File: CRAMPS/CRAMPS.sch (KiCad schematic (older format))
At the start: 11 parts, among them M101 LOGO_OSHW, M102 PCB_GREEN_RMC, P102 RESET, P103 SERIAL0, P104 POWER, Q101 2N7002, SW101 RESET, SW102 POWER, U4 BEAGLEBONEBLACK

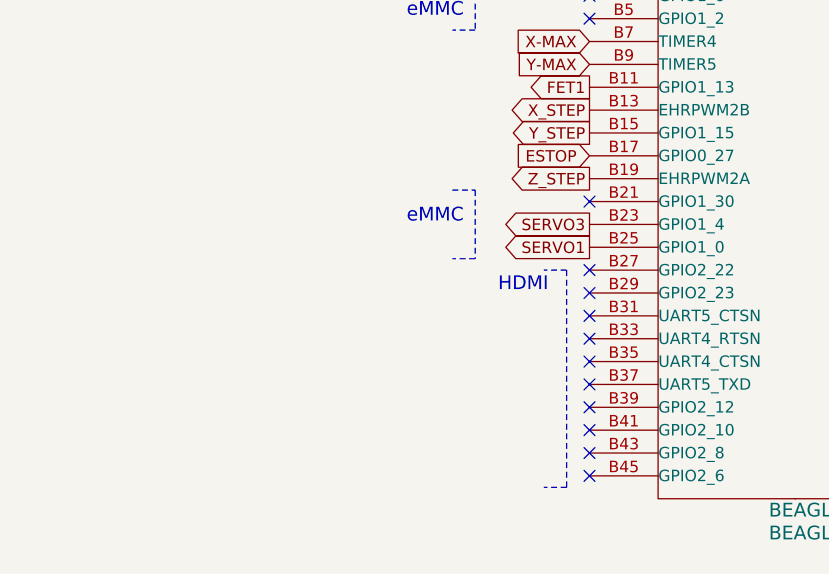
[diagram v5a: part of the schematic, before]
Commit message: Initial BOM files for PCB version 1.0 Added README and ToDo text files
Signed-off-by: Charles Steinkuehler <charles@steinkuehler.net>
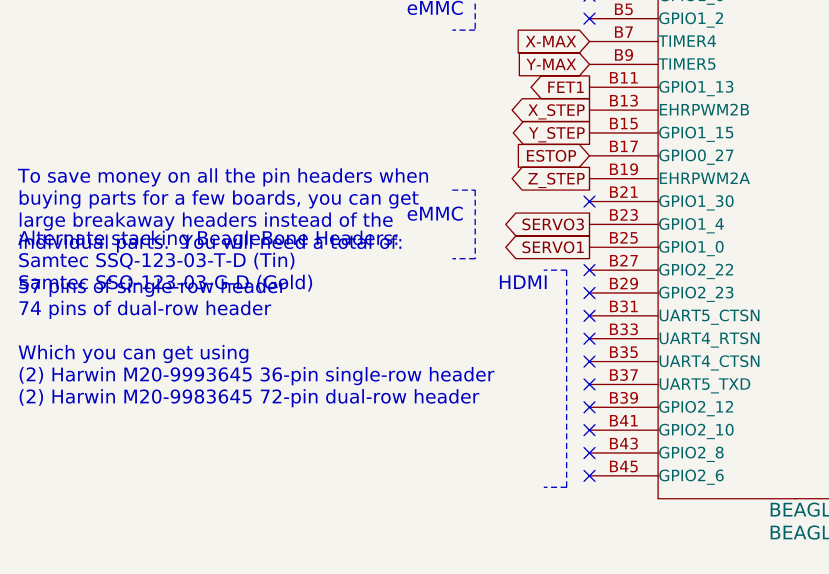
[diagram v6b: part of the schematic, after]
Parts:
- D101: Mfg (none) -> Osram; PartNo (none) -> LG R971-KN-1
- P102, P104: Mfg (none) -> Harwin; PartNo (none) -> M20-9990245
- P103: Mfg (none) -> Harwin; PartNo (none) -> M20-7820646
- Q101: Mfg (none) -> Diodes Inc.; PartNo (none) -> 2N7002K-7
- R101: Mfg (none) -> KOA; PartNo (none) -> RK73H2ATTDD3300F
- SW101, SW102: Mfg (none) -> TE; PartNo (none) -> FSM2JH
- U4: Mfg (none) -> Major League; Note (none) -> 2x required!; PartNo (none) -> SSHQ-123-D-08-GT-LF
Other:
- note added: "Alternate stacking BeagleBone Headers:\nSamtec SSQ-123-03-T-D (Tin)\nSamtec SSQ-123-03-G-D (Gold)\n"
- note added: "To save money on all the pin headers when\nbuying parts for a few boards, you can get\nlarge breakaway headers instead of the\nindividual parts. You will need a total of:\n\n57 pins of single-row header\n74 pins of dual-row header\n\nWhich you can get using\n(2) Harwin M20-9993645 36-pin single-row header\n(2) Harwin M20-9983645 72-pin dual-row header\n"
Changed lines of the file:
@@
 Sheet 1 10
 Title "CRAMPS (Cape-RAMPS for BeagleBone)"
-Date "9 feb 2014"
+Date "11 feb 2014"
 Rev "v1.0"
 Comp ""
@@
 F 2 "" H 10000 5000 60  0001 C CNN
 F 3 "" H 10000 5000 60  0001 C CNN
+F 4 "TE" H 6250 6550 60  0001 C CNN "Mfg"
+F 5 "FSM2JH" H 6250 6550 60  0001 C CNN "PartNo"
 	1    10000 5000
 	0    1    1    0
@@
 F 2 "" H 7900 5000 60  0001 C CNN
 F 3 "" H 7900 5000 60  0001 C CNN
+F 4 "Osram" H 6250 6550 60  0001 C CNN "Mfg"
+F 5 "LG R971-KN-1" H 6250 6550 60  0001 C CNN "PartNo"
 	1    7900 5000
 	0    1    1    0
@@
 F 2 "" H 7900 4450 60  0001 C CNN
 F 3 "" H 7900 4450 60  0001 C CNN
+F 4 "KOA" H 6250 6550 60  0001 C CNN "Mfg"
+F 5 "RK73H2ATTDD3300F" H 6250 6550 60  0001 C CNN "PartNo"
 	1    7900 4450
 	1    0    0    -1
@@
 F 2 "" H 10750 5000 60  0000 C CNN
 F 3 "" H 10750 5000 60  0000 C CNN
+F 4 "Harwin" H 6250 6550 60  0001 C CNN "Mfg"
+F 5 "M20-9990245" H 6250 6550 60  0001 C CNN "PartNo"
 	1    10750 5000
 	1    0    0    -1
@@
 F 2 "~" H 7800 5600 60  0000 C CNN
 F 3 "~" H 7800 5600 60  0000 C CNN
+F 4 "Diodes Inc." H 6250 6550 60  0001 C CNN "Mfg"
+F 5 "2N7002K-7" H 6250 6550 60  0001 C CNN "PartNo"
 	1    7800 5600
 	1    0    0    -1
@@
 F 2 "~" H 3450 600 60  0000 C CNN
 F 3 "~" H 3450 600 60  0000 C CNN
+F 4 "Major League" H 3650 5050 60  0001 C CNN "Mfg"
+F 5 "SSHQ-123-D-08-GT-LF" H 3650 5050 60  0001 C CNN "PartNo"
+F 6 "2x required!" H 3650 5050 60  0001 C CNN "Note"
 	1    3650 1850
 	1    0    0    -1
@@
 F 2 "~" H 4150 600 60  0000 C CNN
 F 3 "~" H 4150 600 60  0000 C CNN
+F 4 "Major League" H 3650 5050 60  0001 C CNN "Mfg"
+F 5 "SSHQ-123-D-08-GT-LF" H 3650 5050 60  0001 C CNN "PartNo"
+F 6 "2x required!" H 3650 5050 60  0001 C CNN "Note"
 	2    4350 1850
 	-1   0    0    -1
@@
 F 2 "~" H 3450 3800 60  0000 C CNN
 F 3 "~" H 3450 3800 60  0000 C CNN
+F 4 "Major League" H 3650 5050 60  0001 C CNN "Mfg"
+F 5 "SSHQ-123-D-08-GT-LF" H 3650 5050 60  0001 C CNN "PartNo"
+F 6 "2x required!" H 3650 5050 60  0001 C CNN "Note"
 	3    3650 5050
 	1    0    0    -1
@@
 F 2 "~" H 4150 3800 60  0000 C CNN
 F 3 "~" H 4150 3800 60  0000 C CNN
+F 4 "Major League" H 3650 5050 60  0001 C CNN "Mfg"
+F 5 "SSHQ-123-D-08-GT-LF" H 3650 5050 60  0001 C CNN "PartNo"
+F 6 "2x required!" H 3650 5050 60  0001 C CNN "Note"
 	4    4350 5050
 	-1   0    0    -1
@@
 F 2 "" H 2050 6950 60  0001 C CNN
 F 3 "" H 2050 6950 60  0001 C CNN
+F 4 "Harwin" H 6250 6550 60  0001 C CNN "Mfg"
+F 5 "M20-7820646" H 6250 6550 60  0001 C CNN "PartNo"
 	1    2050 6950
 	1    0    0    -1
@@
 F 2 "" H 10000 3700 60  0001 C CNN
 F 3 "" H 10000 3700 60  0001 C CNN
+F 4 "TE" H 6250 6550 60  0001 C CNN "Mfg"
+F 5 "FSM2JH" H 6250 6550 60  0001 C CNN "PartNo"
 	1    10000 3700
 	0    1    1    0
@@
 F 2 "" H 10750 3700 60  0000 C CNN
 F 3 "" H 10750 3700 60  0000 C CNN
+F 4 "Harwin" H 6250 6550 60  0001 C CNN "Mfg"
+F 5 "M20-9990245" H 6250 6550 60  0001 C CNN "PartNo"
 	1    10750 3700
 	1    0    0    -1
@@
 NoConn ~ 3100 3000
 NoConn ~ 4900 1700
+Text Notes 600  2200 0    60   ~ 0
+Alternate stacking BeagleBone Headers:\nSamtec SSQ-123-03-T-D (Tin)\nSamtec SSQ-123-03-G-D (Gold)\n
+Text Notes 600  2700 0    60   ~ 0
+To save money on all the pin headers when\nbuying parts for a few boards, you can get\nlarge breakaway headers instead of the\nindividual parts.  You will need a total of:\n\n57 pins of single-row header\n74 pins of dual-row header\n\nWhich you can get using\n(2) Harwin M20-9993645 36-pin single-row header\n(2) Harwin M20-9983645 72-pin dual-row header\n
 $EndSCHEMATC

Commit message: BOM Updates Fixed incorrect Molex part number Added Stackpole resistor part numbers Switched to value-sorted BOM export from KiCAD Modified some attribute fields to get same-value parts to list on a single BOM line
Signed-off-by: Charles Steinkuehler <charles@steinkuehler.net>
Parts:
- R101: AltMfg (none) -> KOA; AltPartNo (none) -> RK73H2ATTDD3300F; Mfg KOA -> Stackpole; PartNo RK73H2ATTDD3300F -> RMCF0805FT330R
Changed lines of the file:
@@
 Sheet 1 10
 Title "CRAMPS (Cape-RAMPS for BeagleBone)"
-Date "11 feb 2014"
+Date "15 feb 2014"
 Rev "v1.0"
 Comp ""
@@
 F 2 "OSHW_logo_2" H 6000 7250 60  0000 C CNN
 F 3 "" H 6100 7200 60  0001 C CNN
-	1    6100 7200
-	1    0    0    -1
+    1    6100 7200
+    1    0    0    -1
 $EndComp
 Text GLabel 4900 5900 2    50   Input ~ 0
@@
 F 2 "" H 10000 5500 60  0001 C CNN
 F 3 "" H 10000 5500 60  0001 C CNN
-	1    10000 5500
-	1    0    0    -1
+    1    10000 5500
+    1    0    0    -1
 $EndComp
 $Comp
@@
 F 4 "TE" H 6250 6550 60  0001 C CNN "Mfg"
 F 5 "FSM2JH" H 6250 6550 60  0001 C CNN "PartNo"
-	1    10000 5000
-	0    1    1    0
+    1    10000 5000
+    0    1    1    0
 $EndComp
 $Comp
@@
 F 2 "" H 7900 6000 60  0001 C CNN
 F 3 "" H 7900 6000 60  0001 C CNN
-	1    7900 6000
-	1    0    0    -1
+    1    7900 6000
+    1    0    0    -1
 $EndComp
 $Comp
@@
 F 4 "Osram" H 6250 6550 60  0001 C CNN "Mfg"
 F 5 "LG R971-KN-1" H 6250 6550 60  0001 C CNN "PartNo"
-	1    7900 5000
-	0    1    1    0
+    1    7900 5000
+    0    1    1    0
 $EndComp
 $Comp
@@
 F 2 "" H 7900 4450 60  0001 C CNN
 F 3 "" H 7900 4450 60  0001 C CNN
-F 4 "KOA" H 6250 6550 60  0001 C CNN "Mfg"
-F 5 "RK73H2ATTDD3300F" H 6250 6550 60  0001 C CNN "PartNo"
-	1    7900 4450
-	1    0    0    -1
+F 4 "Stackpole" H 6250 6550 60  0001 C CNN "Mfg"
+F 5 "RMCF0805FT330R" H 6250 6550 60  0001 C CNN "PartNo"
+F 6 "KOA" H 6250 6550 60  0001 C CNN "AltMfg"
+F 7 "RK73H2ATTDD3300F" H 6250 6550 60  0001 C CNN "AltPartNo"
+    1    7900 4450
+    1    0    0    -1
 $EndComp
 $Comp
@@
 F 2 "" H 5200 7200 60  0000 C CNN
 F 3 "" H 5200 7200 60  0000 C CNN
-	1    5200 7200
-	1    0    0    -1
+    1    5200 7200
+    1    0    0    -1
 $EndComp
 Text GLabel 4900 5300 2    50   Output ~ 0
@@
 F 4 "Harwin" H 6250 6550 60  0001 C CNN "Mfg"
 F 5 "M20-9990245" H 6250 6550 60  0001 C CNN "PartNo"
-	1    10750 5000
-	1    0    0    -1
+    1    10750 5000
+    1    0    0    -1
 $EndComp
 $Sheet
@@
 F 2 "" H 7900 4100 60  0000 C CNN
 F 3 "" H 7900 4100 60  0000 C CNN
-	1    7900 4100
-	1    0    0    -1
+    1    7900 4100
+    1    0    0    -1
 $EndComp
 $Comp
@@
 F 4 "Diodes Inc." H 6250 6550 60  0001 C CNN "Mfg"
 F 5 "2N7002K-7" H 6250 6550 60  0001 C CNN "PartNo"
-	1    7800 5600
-	1    0    0    -1
+    1    7800 5600
+    1    0    0    -1
 $EndComp
 Text Notes 5050 2200 0    60   ~ 0
@@
 F 5 "SSHQ-123-D-08-GT-LF" H 3650 5050 60  0001 C CNN "PartNo"
 F 6 "2x required!" H 3650 5050 60  0001 C CNN "Note"
-	1    3650 1850
-	1    0    0    -1
+    1    3650 1850
+    1    0    0    -1
 $EndComp
 $Comp
@@
 F 5 "SSHQ-123-D-08-GT-LF" H 3650 5050 60  0001 C CNN "PartNo"
 F 6 "2x required!" H 3650 5050 60  0001 C CNN "Note"
-	2    4350 1850
-	-1   0    0    -1
+    2    4350 1850
+    -1   0    0    -1
 $EndComp
 $Comp
@@
 F 5 "SSHQ-123-D-08-GT-LF" H 3650 5050 60  0001 C CNN "PartNo"
 F 6 "2x required!" H 3650 5050 60  0001 C CNN "Note"
-	3    3650 5050
-	1    0    0    -1
+    3    3650 5050
+    1    0    0    -1
 $EndComp
 $Comp
@@
 F 5 "SSHQ-123-D-08-GT-LF" H 3650 5050 60  0001 C CNN "PartNo"
 F 6 "2x required!" H 3650 5050 60  0001 C CNN "Note"
-	4    4350 5050
-	-1   0    0    -1
+    4    4350 5050
+    -1   0    0    -1
 $EndComp
 Text GLabel 3100 5100 0    50   Output ~ 0
@@
 F 4 "Harwin" H 6250 6550 60  0001 C CNN "Mfg"
 F 5 "M20-7820646" H 6250 6550 60  0001 C CNN "PartNo"
-	1    2050 6950
-	1    0    0    -1
+    1    2050 6950
+    1    0    0    -1
 $EndComp
 $Comp
@@
 F 2 "" H 1600 7300 60  0001 C CNN
 F 3 "" H 1600 7300 60  0001 C CNN
-	1    1600 7300
-	1    0    0    -1
-$EndComp
-Wire Wire Line
-	10000 5300 10000 5500
-Wire Wire Line
-	7900 5800 7900 6000
-Wire Wire Line
-	7900 4800 7900 4700
-Wire Wire Line
-	9800 4600 10400 4600
-Wire Wire Line
-	10000 4600 10000 4700
-Wire Notes Line
-	6500 650  6500 7600
-Wire Wire Line
-	10400 4600 10400 4900
+    1    1600 7300
+    1    0    0    -1
+$EndComp
+Wire Wire Line
+    10000 5300 10000 5500
+Wire Wire Line
+    7900 5800 7900 6000
+Wire Wire Line
+    7900 4800 7900 4700
+Wire Wire Line
+    9800 4600 10400 4600
+Wire Wire Line
+    10000 4600 10000 4700
+Wire Notes Line
+    6500 650  6500 7600
+Wire Wire Line
+    10400 4600 10400 4900
 Connection ~ 10000 4600
 Wire Wire Line
-	10400 5100 10400 5400
-Wire Wire Line
-	10400 5400 10000 5400
+    10400 5100 10400 5400
+Wire Wire Line
+    10400 5400 10000 5400
 Connection ~ 10000 5400
 Wire Wire Line
-	7900 4100 7900 4200
-Wire Wire Line
-	7900 5400 7900 5200
-Wire Notes Line
-	5500 850  5400 850
-Wire Notes Line
-	5400 850  5400 1050
-Wire Notes Line
-	5400 1050 5500 1050
-Wire Notes Line
-	2500 850  2600 850
-Wire Notes Line
-	2600 850  2600 1050
-Wire Notes Line
-	2600 1050 2500 1050
-Wire Notes Line
-	5500 1650 5400 1650
-Wire Notes Line
-	5400 1650 5400 1950
-Wire Notes Line
-	5400 1950 5500 1950
-Wire Notes Line
-	2500 1750 2600 1750
-Wire Notes Line
-	3000 2100 3000 3050
-Wire Notes Line
-	5000 3050 5100 3050
-Wire Notes Line
-	3000 3050 2900 3050
-Wire Notes Line
-	3000 2100 2900 2100
-Wire Notes Line
-	5000 2100 5000 3050
-Wire Notes Line
-	5000 2100 5100 2100
-Wire Wire Line
-	1700 6700 1600 6700
-Wire Wire Line
-	1600 6700 1600 7300
-Wire Wire Line
-	1500 7000 1700 7000
-Wire Wire Line
-	1700 7100 1500 7100
+    7900 4100 7900 4200
+Wire Wire Line
+    7900 5400 7900 5200
+Wire Notes Line
+    5500 850  5400 850
+Wire Notes Line
+    5400 850  5400 1050
+Wire Notes Line
+    5400 1050 5500 1050
+Wire Notes Line
+    2500 850  2600 850
+Wire Notes Line
+    2600 850  2600 1050
+Wire Notes Line
+    2600 1050 2500 1050
+Wire Notes Line
+    5500 1650 5400 1650
+Wire Notes Line
+    5400 1650 5400 1950
+Wire Notes Line
+    5400 1950 5500 1950
+Wire Notes Line
+    2500 1750 2600 1750
+Wire Notes Line
+    3000 2100 3000 3050
+Wire Notes Line
+    5000 3050 5100 3050
+Wire Notes Line
+    3000 3050 2900 3050
+Wire Notes Line
+    3000 2100 2900 2100
+Wire Notes Line
+    5000 2100 5000 3050
+Wire Notes Line
+    5000 2100 5100 2100
+Wire Wire Line
+    1700 6700 1600 6700
+Wire Wire Line
+    1600 6700 1600 7300
+Wire Wire Line
+    1500 7000 1700 7000
+Wire Wire Line
+    1700 7100 1500 7100
 Text GLabel 4900 4300 2    50   UnSpc ~ 0
 SYS_5V
@@
 F 2 "" H 10000 4200 60  0001 C CNN
 F 3 "" H 10000 4200 60  0001 C CNN
-	1    10000 4200
-	1    0    0    -1
+    1    10000 4200
+    1    0    0    -1
 $EndComp
 $Comp
@@
 F 4 "TE" H 6250 6550 60  0001 C CNN "Mfg"
 F 5 "FSM2JH" H 6250 6550 60  0001 C CNN "PartNo"
-	1    10000 3700
-	0    1    1    0
+    1    10000 3700
+    0    1    1    0
 $EndComp
 $Comp
@@
 F 4 "Harwin" H 6250 6550 60  0001 C CNN "Mfg"
 F 5 "M20-9990245" H 6250 6550 60  0001 C CNN "PartNo"
-	1    10750 3700
-	1    0    0    -1
-$EndComp
-Wire Wire Line
-	10000 4000 10000 4200
-Wire Wire Line
-	10000 3300 10000 3400
-Wire Wire Line
-	10400 3300 10400 3600
-Wire Wire Line
-	10400 3800 10400 4100
-Wire Wire Line
-	10400 4100 10000 4100
+    1    10750 3700
+    1    0    0    -1
+$EndComp
+Wire Wire Line
+    10000 4000 10000 4200
+Wire Wire Line
+    10000 3300 10000 3400
+Wire Wire Line
+    10400 3300 10400 3600
+Wire Wire Line
+    10400 3800 10400 4100
+Wire Wire Line
+    10400 4100 10000 4100
 Connection ~ 10000 4100
 Wire Wire Line
-	9800 3300 10400 3300
+    9800 3300 10400 3300
 Connection ~ 10000 3300
 Text GLabel 7500 5600 0    50   Output ~ 0
 LED
 Wire Wire Line
-	7600 5600 7500 5600
+    7600 5600 7500 5600
 Text GLabel 9800 4600 0    50   Output ~ 0
 /RESET
@@
 DGND
 Wire Wire Line
-	3100 6900 3300 6900
-Wire Wire Line
-	3300 6900 3300 7000
+    3100 6900 3300 6900
+Wire Wire Line
+    3300 6900 3300 7000
 $Comp
 L PWR_FLAG #FLG06
@@
 F 2 "" H 3300 6900 60  0001 C CNN
 F 3 "" H 3300 6900 60  0001 C CNN
-	1    3300 6900
-	1    0    0    -1
+    1    3300 6900
+    1    0    0    -1
 $EndComp
 $Comp
@@
 F 2 "" H 3300 7000 60  0001 C CNN
 F 3 "" H 3300 7000 60  0001 C CNN
-	1    3300 7000
-	1    0    0    -1
+    1    3300 7000
+    1    0    0    -1
 $EndComp
 Text GLabel 3100 6900 0    50   UnSpc ~ 0
 DGND
 Wire Notes Line
-	2600 1750 2600 2050
-Wire Notes Line
-	2600 2050 2500 2050
+    2600 1750 2600 2050
+Wire Notes Line
+    2600 2050 2500 2050
 NoConn ~ 3100 900
 NoConn ~ 3100 1000
